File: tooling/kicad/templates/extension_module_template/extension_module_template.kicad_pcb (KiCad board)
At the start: 2 copper layers, 130 x 85 mm, 6 parts, among them J1 Conn_01x07_Socket, J2 Conn_01x07_Socket, SW1 SW_DIP_x03

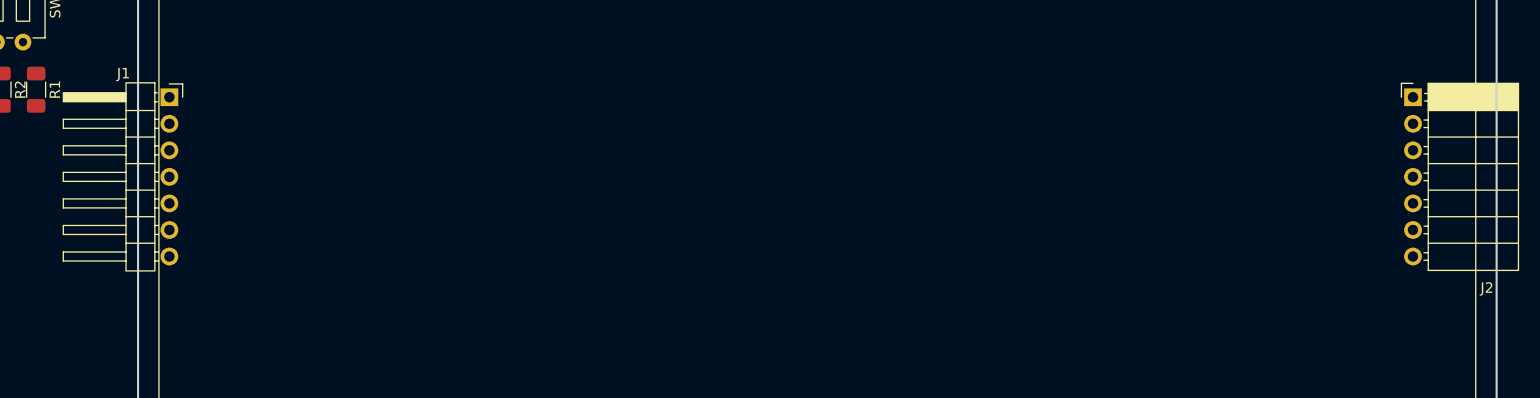
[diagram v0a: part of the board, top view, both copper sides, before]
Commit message: [ADD] board connector
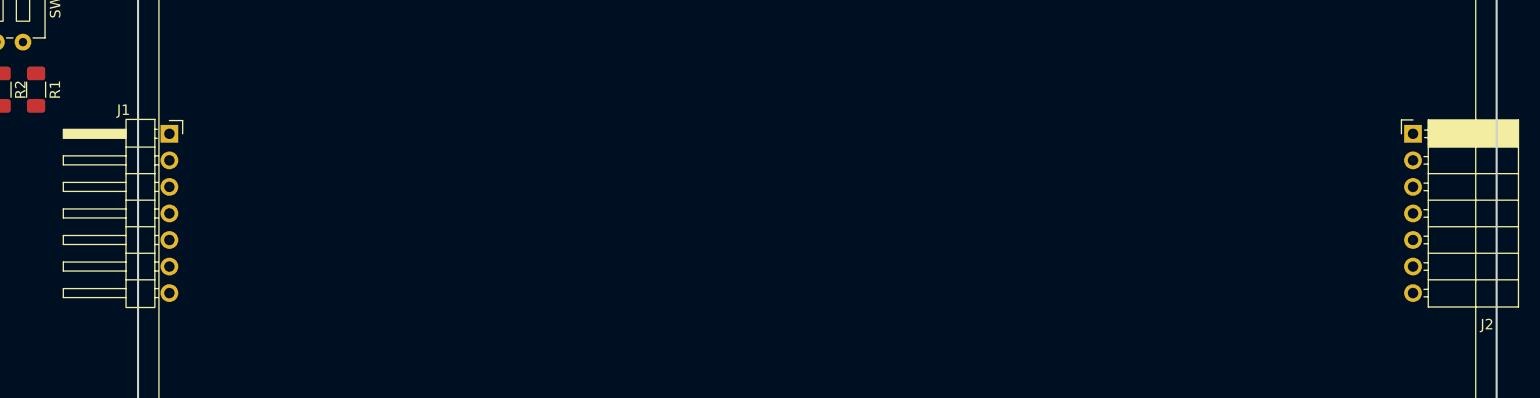
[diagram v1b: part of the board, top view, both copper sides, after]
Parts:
- moved J1 3.50 mm to (88.0, 83.5)
- moved J2 3.50 mm to (207.0, 83.5)
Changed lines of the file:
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@@
 		(locked yes)
 		(layer "F.Cu")
-		(at 207 80)
+		(at 207 83.5)
 		(descr "Through hole angled socket strip, 1x07, 2.54mm pitch, 8.51mm socket length, single row (from Kicad 4.0.7), script generated")
 		(tags "Through hole angled socket strip THT 1x07 2.54mm single row")
@@
 		(locked yes)
 		(layer "F.Cu")
-		(at 88 80)
+		(at 88 83.5)
 		(descr "Through hole angled pin header, 1x07, 2.54mm pitch, 6mm pin length, single row")
 		(tags "Through hole angled pin header THT 1x07 2.54mm single row")
